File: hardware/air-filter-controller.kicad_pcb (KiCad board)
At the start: 4 copper layers, 41.1 x 138.8 mm, 126 parts, among them J1 TYPE-C-31-M-12, J10 Conn_01x04, J11 Conn_01x04, J12 Conn_01x04, J13 Conn_01x02, J14 Conn_01x02, J3 Conn_01x04, J4 Conn_01x03, J5 Conn_01x04, J6 Conn_01x04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

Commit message: Routing and placement done
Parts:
- added J2: Conn_01x05, Connector_PinHeader_2.54mm:PinHeader_1x05_P2.54mm_Vertical, F.Cu at (143.1, 72.1)
- moved H3 143.7 mm to (107.0, 176.8)
- moved J8 128.5 mm to (109.7, 169.8)
- moved H4 127.6 mm to (141.8, 176.8)
- moved J7 127.2 mm to (109.7, 157.8)
- moved R23 124.5 mm to (105.8, 153.3), turned to 180 degrees
- moved R26 123.8 mm to (105.8, 165.3), turned to 180 degrees
- moved R24 122.6 mm to (111.2, 165.3)
- moved R21 122.5 mm to (111.2, 153.3)
- moved R22 120.6 mm to (108.5, 153.5), turned to 180 degrees
- moved R25 120.1 mm to (108.5, 165.5), turned to 180 degrees
- moved D14 114.8 mm to (107.6, 150.7), turned to 180 degrees
- moved D17 114.4 mm to (107.6, 162.7), turned to 180 degrees
- moved D16 114.2 mm to (114.8, 162.7)
- moved D13 113.2 mm to (114.8, 150.7)
- moved R35 111.0 mm to (132.8, 146.8), turned to 90 degrees
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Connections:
- U1 pad 22: /SDI -> /SDO
- U1 pad 25: unconnected-(U1-IO48-Pad25) -> /PWM0
- U1 pad 32: unconnected-(U1-IO39-Pad32) -> /PWM1
- U1 pad 36: unconnected-(U1-RXD0-Pad36) -> /RXD0
- U1 pad 37: unconnected-(U1-TXD0-Pad37) -> /TXD0
- U1 pad 8: /SDO -> /SDI
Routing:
- net +12V: track 19.8 -> 355.1 mm, vias 0 -> 14
- net +3V3: track 32.7 -> 298.2 mm, vias 0 -> 23
- net /FAN_GND: track 4.49 -> 235.2 mm, vias 0 -> 9
- net /PWM0: track 3.95 -> 132.9 mm, vias 0 -> 4
- net /PWM1: track 0.00 -> 122.9 mm, vias 0 -> 2
- net /TACH4: track 0.00 -> 121.4 mm, vias 0 -> 4
- net /TACH3: track 0.00 -> 114.1 mm, vias 0 -> 4
- net /TACH8: track 0.00 -> 108.1 mm, vias 0 -> 6
- net /TACH2: track 0.00 -> 102.2 mm, vias 0 -> 4
- net GND: track 24.5 -> 122.2 mm, vias 0 -> 413
- net /TACH7: track 0.00 -> 94.6 mm, vias 0 -> 4
- net /TACH1: track 0.00 -> 90.0 mm, vias 0 -> 4
- net /TACH6: track 0.00 -> 84.8 mm, vias 0 -> 6
- net /TACH5: track 0.00 -> 73.1 mm, vias 0 -> 4
- net /TACH0: track 4.99 -> 71.6 mm, vias 0 -> 2
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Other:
- board size 41.1 x 138.8 mm -> 41 x 134.6 mm
- board text added: "air-filter-controller v1.0"

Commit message: Hardware v1.0
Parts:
- C8: value 47uF -> 22uF 25V
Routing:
- net Net-(U3-EN): track 2.82 -> 5.82 mm
- net GND: track 122.2 -> 121.3 mm
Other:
- board text added: "0"
- board text added: "1"
- board text added: "12V"
- board text added: "2"
- board text added: "3"
- board text added: "3V3"
- board text added: "4"
- board text added: "5"
- board text added: "5V-12V in 5.5mm/2.1mm Center positive"
- board text added: "6"
- board text added: "7"
- board text added: "8"
- board text added: "G"
- board text added: "GND"
- board text added: "JACK"
- board text added: "M3 x4"
- board text added: "POWER"
- board text added: "PWM"
- board text added: "RX"
- board text added: "SW2"
- board text added: "SW3"
- board text added: "TACH"
- board text added: "TX"
- board text added: "USB"

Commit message: v1.1: start updating layout
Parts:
- removed C6: 100nF, Capacitor_SMD:C_0402_1005Metric
- removed LED1: HL-AF-5060H271BU46FU79GC-S1-THL, Homebrew:LED-ARRAY-SMD_6P-L5.4-W5.0-TL-FD
- removed U2: BMP280, Package_LGA:Bosch_LGA-8_2x2.5mm_P0.65mm_ClockwisePinNumbering
- added C14: 100nF, Capacitor_SMD:C_0402_1005Metric, F.Cu at (136.4, 60.1)
- added C15: 47uF, Capacitor_SMD:C_1206_3216Metric, F.Cu at (132.6, 90.0)
- added C16: 100nF, Capacitor_SMD:C_0402_1005Metric, F.Cu at (134.3, 90.0)
- added C17: 47uF, Capacitor_SMD:C_1206_3216Metric, F.Cu at (97.6, 82.8)
- added C18: 100nF, Capacitor_SMD:C_0402_1005Metric, F.Cu at (91.5, 84.8)
- added D37: WS2812B-2020, Homebrew:LED-SMD_4P-L2.0-W2.0-TL_WS2812B-2020, F.Cu at (136.8, 52.6)
- added D38: WS2812B-2020, Homebrew:LED-SMD_4P-L2.0-W2.0-TL_WS2812B-2020, F.Cu at (136.8, 55.5)
- added D39: WS2812B-2020, Homebrew:LED-SMD_4P-L2.0-W2.0-TL_WS2812B-2020, F.Cu at (136.8, 58.2)
- added D40: SMAJ5.0A, Diode_SMD:D_SMA, F.Cu at (173.5, 126.2)
- added D41: SMAJ5.0A, Diode_SMD:D_SMA, F.Cu at (140.2, 89.9)
- added D42: D, Diode_SMD:D_SMA, F.Cu at (173.5, 135.3)
- added D43: SMAJ5.0A, Diode_SMD:D_SMA, F.Cu at (133.8, 190.7)
- added D44: SMAJ5.0A, Diode_SMD:D_SMA, F.Cu at (130.1, 196.4)
- added D45: D_TVS 12V, Diode_SMD:D_SMA, F.Cu at (141.1, 191.8)
- added H5: Strain Relief, Homebrew:3_pin_2.54mm_pitch_strain_relief, F.Cu at (143.6, 90.0)
- added J15: Conn_01x03, Connector_PinHeader_2.54mm:PinHeader_1x03_P2.54mm_Vertical, F.Cu at (136.6, 87.4)
- added J16: Conn_01x08, easyeda2kicad:CONN-TH_8P-P1.25_HCTL_HC-1.25-8A, F.Cu at (184.0, 125.8)
- added J17: Conn_01x08, easyeda2kicad:CONN-TH_8P-P1.25_HCTL_HC-1.25-8A, F.Cu at (184.0, 130.2)
- added R48: 100, Resistor_SMD:R_0603_1608Metric_Pad0.98x0.95mm_HandSolder, F.Cu at (167.2, 125.2)
- added R49: 100, Resistor_SMD:R_0603_1608Metric_Pad0.98x0.95mm_HandSolder, F.Cu at (167.2, 127.7)
- added R50: 100, Resistor_SMD:R_0603_1608Metric_Pad0.98x0.95mm_HandSolder, F.Cu at (167.2, 130.2)
- added R51: 100, Resistor_SMD:R_0603_1608Metric_Pad0.98x0.95mm_HandSolder, F.Cu at (167.2, 132.7)
- added R52: 100, Resistor_SMD:R_0603_1608Metric_Pad0.98x0.95mm_HandSolder, F.Cu at (167.2, 135.2)
- added R53: 100, Resistor_SMD:R_0603_1608Metric_Pad0.98x0.95mm_HandSolder, F.Cu at (167.2, 137.7)
- added U4: AMS1117-3.3, Package_TO_SOT_SMD:SOT-223-3_TabPin2, F.Cu at (91.0, 90.8)
- added U5: ZX-SH1.0-4PWT, easyeda2kicad:CONN-SMD_4P-P1.00_MEGASTAR_ZX-SH1.0-4PWT, F.Cu at (173.2, 140.6)
- D35: value SMAJ5.0A -> WS2812B-2020; footprint Diode_SMD:D_SMA -> Homebrew:LED-SMD_4P-L2.0-W2.0-TL_WS2812B-2020
- J4: value Conn_01x03 -> Conn_01x04; footprint Connector_PinHeader_2.54mm:PinHeader_1x03_P2.54mm_Vertical -> Homebrew:CONN-TH_47053-1000
- L1: value 27uH -> 100uH
- R3: value 10 -> 220
- R4: value 10 -> 100k
- R46: value 47 -> 220
- R5: value 10 -> 1k; footprint Resistor_SMD:R_0603_1608Metric_Pad0.98x0.95mm_HandSolder -> Resistor_SMD:R_0402_1005Metric
- R8: value 22k 1% -> 16k 1%
- R9: value 100k 1% -> 110k 1%
- moved R4 140.6 mm to (132.7, 194.9), turned to -90 degrees
- moved R5 140.3 mm to (136.5, 193.0)
- moved R46 131.9 mm to (132.7, 198.3), turned to 90 degrees
- moved J4 121.9 mm to (139.1, 197.3), turned to 0 degrees
- moved D35 54.1 mm to (136.7, 49.9), turned to 0 degrees
- moved C7 42.4 mm to (88.2, 84.3), turned to -90 degrees
- moved D21 27.5 mm to (141.1, 143.8)
- moved D33 27.5 mm to (110.8, 136.3)
- moved D34 27.5 mm to (138.0, 136.3)
- moved J5 27.5 mm to (109.6, 149.3)
- moved J9 27.5 mm to (139.1, 149.3)
- moved R14 27.5 mm to (105.7, 144.8)
- moved R15 27.5 mm to (111.1, 144.8)
- moved R44 27.5 mm to (108.5, 135.1)
- moved D10 27.5 mm to (114.7, 166.2)
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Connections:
- BUZZER1 pad 1: Net-(BUZZER1-Pad1) -> /BUZZER
- C10 pad 2: +3V3 -> +5V
- C11 pad 1: +3V3 -> +5V
- C12 pad 1: +3V3 -> +5V
- C7 pad 1: GND -> +5V
- C7 pad 2: +3V3 -> GND
- D35 pad 1: /BOOT -> +5V
- D35 pad 2: GND -> Net-(D35-DOUT)
- F1 pad 1: Net-(J4-Pin_2) -> /12V_RAW
- J2 pad 5: +12V -> +5V
- J4 pad 1: /12V_RAW -> /FAN_GND
- J4 pad 2: Net-(J4-Pin_2) -> +12V
- J4 pad 3: /VBUS_RAW -> Net-(J4-Pin_3)
- L1 pad 2: +3V3 -> +5V
- R3 pad 1: /LED_G -> Net-(D39-DOUT)
- R3 pad 2: Net-(LED1-A-Pad1) -> /LED_OUT
- R4 pad 1: /LED_R -> /TACH9
- R4 pad 2: Net-(LED1-A-Pad2) -> +3V3
- R46 pad 1: Net-(BUZZER1-Pad1) -> /PWM1
- R46 pad 2: /BUZZER -> Net-(J4-Pin_4)
- R5 pad 1: /LED_B -> /TACH9
- R5 pad 2: Net-(LED1-A-Pad3) -> Net-(J4-Pin_3)
- R9 pad 1: +3V3 -> +5V
- U1 pad 10: /12V_DIVIDED -> /PM0_RX
- U1 pad 13: /USB_DP -> /USB_DN
- U1 pad 14: /USB_DN -> /USB_DP
- U1 pad 16: unconnected-(U1-IO46-Pad16) -> /PM_SENSOR_ENABLE
- U1 pad 21: /SCK -> /TACH9
- U1 pad 22: /SDO -> /PM0_TX
- U1 pad 26: unconnected-(U1-IO45-Pad26) -> /SW0
- U1 pad 33: /LED_G -> /LED_SIGNAL
- U1 pad 34: /LED_R -> /SDA
- U1 pad 35: /LED_B -> /SCL
- U1 pad 39: /SW0 -> /12V_DIVIDED
- U1 pad 8: /SDI -> /PM1_RX
- U1 pad 9: /CSB -> /PM1_TX
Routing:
- net +3V3: track 298.2 -> 168.9 mm, vias 23 -> 20
- net /TACH9: track 0.00 -> 118.1 mm, vias 0 -> 4
- net +5V: track 0.00 -> 92.9 mm, vias 0 -> 6
- net /BOOT: track 56.7 -> 0.00 mm, vias 4 -> 0
- net /SW0: track 56.0 -> 3.84 mm, vias 2 -> 0
- net Net-(Q1-G): track 46.2 -> 0.00 mm, vias 4 -> 0
- net /LED_OUT: track 0.00 -> 34.9 mm, vias 0 -> 2
- net /SW1: track 56.8 -> 24.7 mm, vias 2 -> 1
- net /TXD0: track 27.9 -> 0.00 mm, vias 1 -> 0
- net /FAN_GND: track 235.2 -> 261.2 mm, vias 9 -> 10
- net +12V: track 355.1 -> 329.8 mm, vias 14 -> 10
- net /SDI: track 23.6 -> 0.00 mm, vias 2 -> 0
- net /CSB: track 21.9 -> 0.00 mm, vias 2 -> 0
- net /RXD0: track 27.2 -> 5.84 mm, vias 2 -> 1
- net GND: track 121.3 -> 141.5 mm, vias 413 -> 47
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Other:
- board size 41 x 134.6 mm -> 41.1 x 163.6 mm
- board text added: "9"
- board text added: "air-filter-controller v1.1"
- board text removed: "air-filter-controller v1.0"

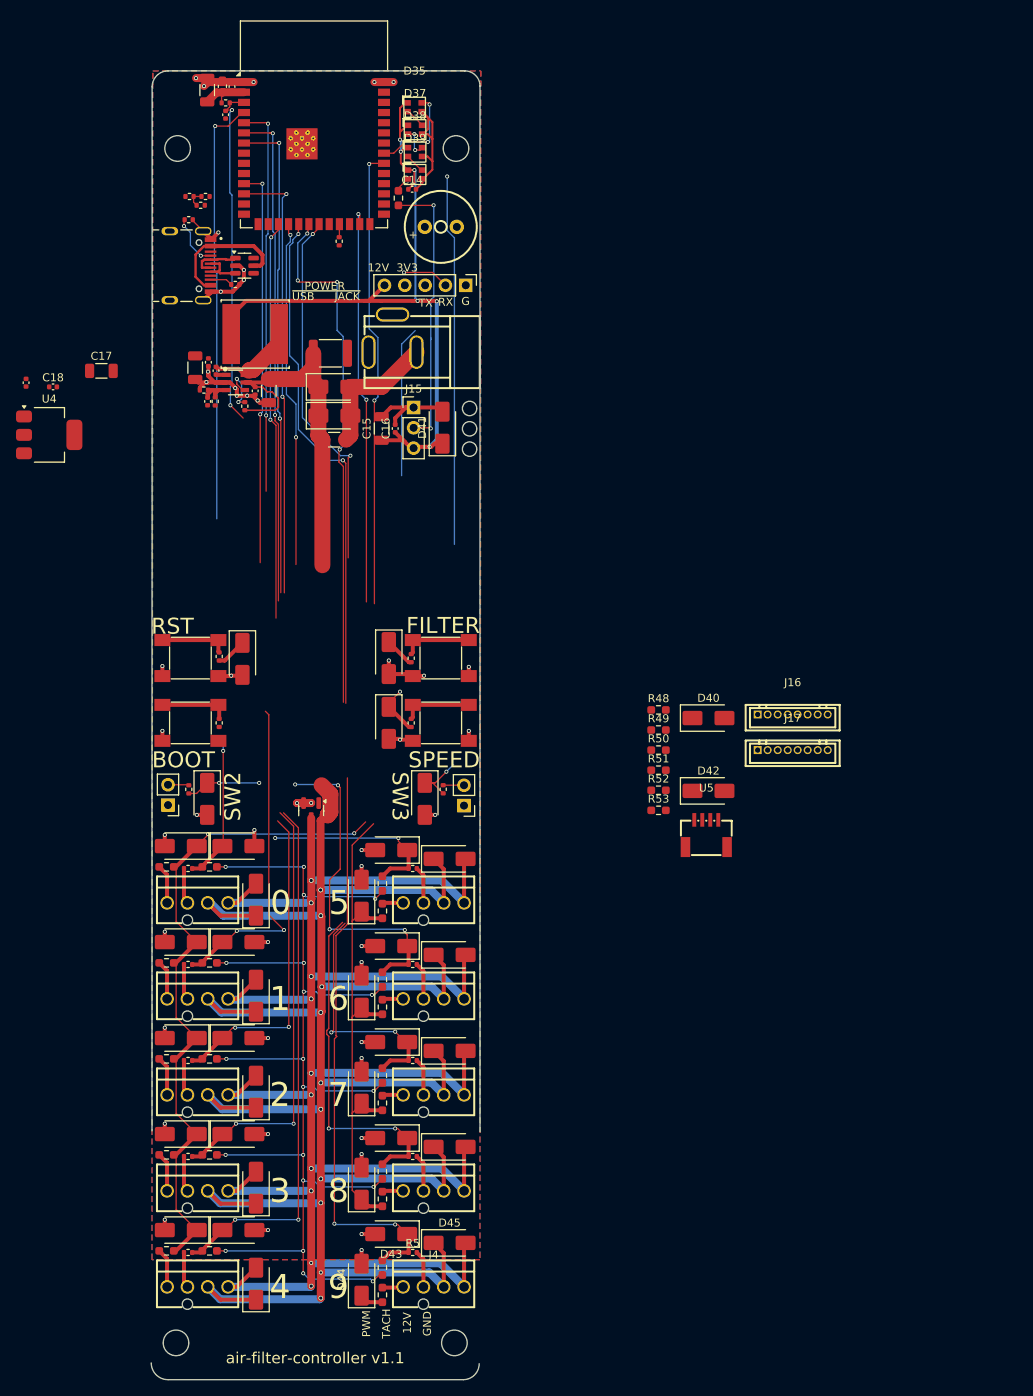
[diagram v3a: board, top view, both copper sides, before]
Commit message: Hardware revision v1.1:
- Fix flipped USB lines
- Remove diode on BOOT switch
- Remove buzzer resistor
- Change voltage divider to ADC channel 1
- Increased from 9 to 10 fan channels
- Switched to addressable LEDs
- Added connector for offboard WS2812 LEDs
- Added a Qwiic connector
- Added two connectors for PMS5003 particle sensors
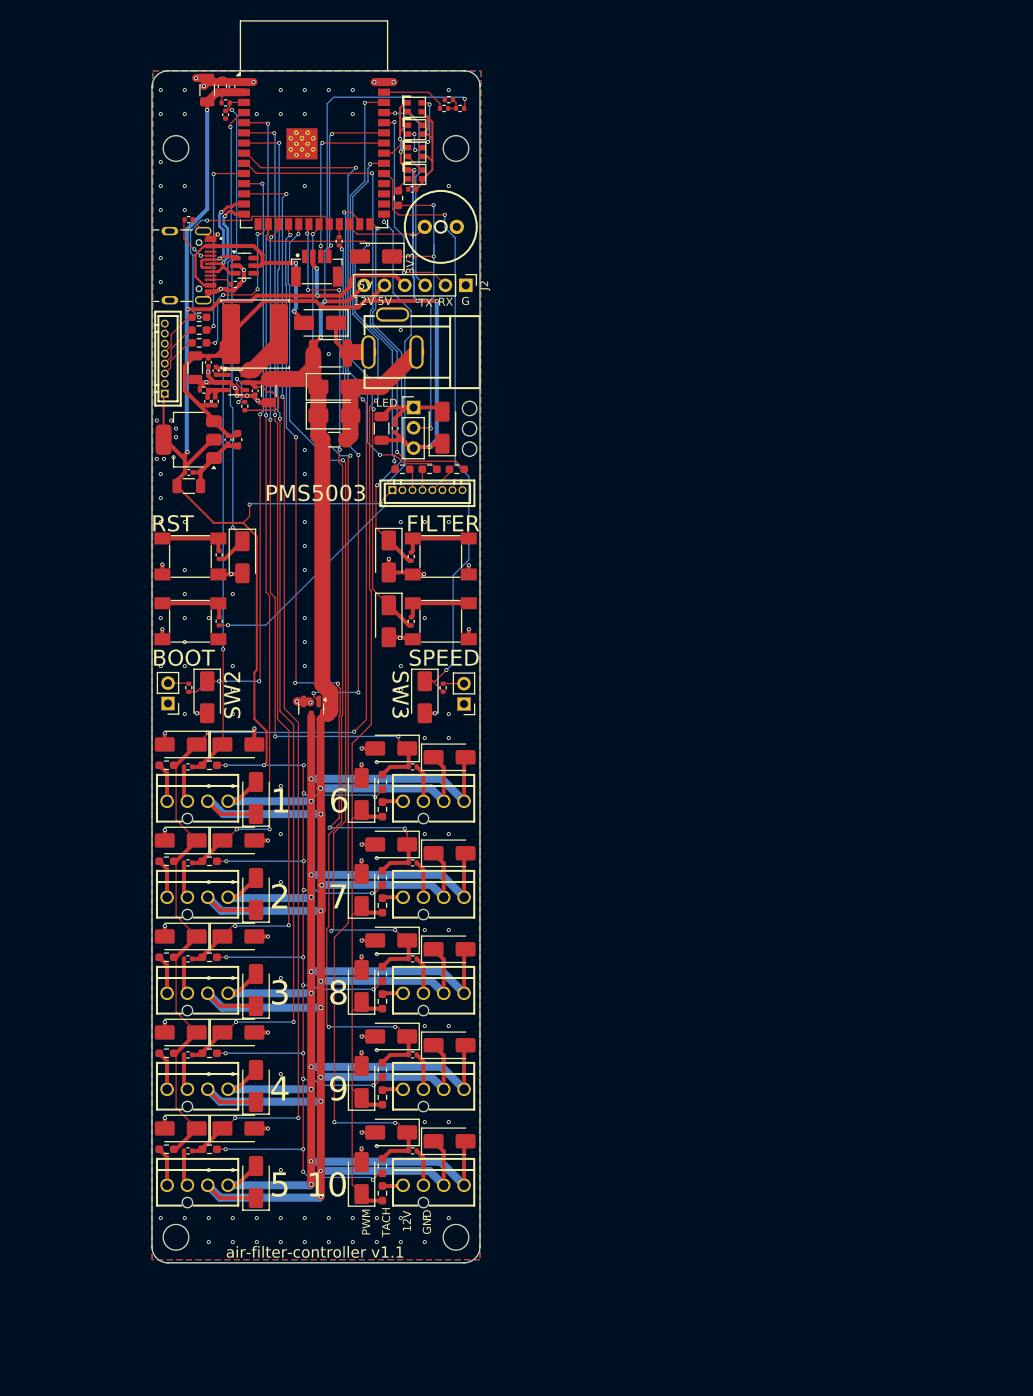
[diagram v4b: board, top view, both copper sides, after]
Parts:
- added C6: 10uF, Capacitor_SMD:C_0603_1608Metric, F.Cu at (114.6, 91.4)
- J16, J17: footprint easyeda2kicad:CONN-TH_8P-P1.25_HCTL_HC-1.25-8A -> Homebrew:CONN-TH_8P-P1.25_HCTL_HC-1.25-8A
- J2: value Conn_01x05 -> Conn_01x06; footprint Connector_PinHeader_2.54mm:PinHeader_1x05_P2.54mm_Vertical -> Connector_PinHeader_2.54mm:PinHeader_1x06_P2.54mm_Vertical
- U5: value ZX-SH1.0-4PWT -> HC-1.0-4PLT; footprint easyeda2kicad:CONN-SMD_4P-P1.00_MEGASTAR_ZX-SH1.0-4PWT -> Homebrew:CONN-SMD_4P-P1.00_HC-1.0-4PLT
- moved J16 90.2 mm to (105.5, 81.3), turned to 90 degrees
- moved U5 86.0 mm to (124.5, 69.8)
- moved R50 78.9 mm to (109.8, 76.1), turned to 180 degrees
- moved R49 76.1 mm to (109.8, 77.7), turned to 180 degrees
- moved D42 76.0 mm to (124.9, 76.8), turned to 180 degrees
- moved R48 73.5 mm to (109.8, 79.3), turned to 180 degrees
- moved D40 71.1 mm to (131.9, 68.5), turned to 180 degrees
- moved J17 56.0 mm to (138.3, 97.7)
- moved R53 49.5 mm to (142.0, 95.1), turned to 180 degrees
- moved R51 49.4 mm to (135.2, 95.1)
- moved R52 49.3 mm to (138.6, 95.1), turned to 180 degrees
- moved R41 35.6 mm to (142.4, 50.0), turned to 180 degrees
- moved R42 33.7 mm to (141.0, 48.9), turned to 180 degrees
- moved R43 31.8 mm to (140.4, 50.0), turned to 180 degrees
- moved C7 26.2 mm to (113.4, 91.4)
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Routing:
- net +3V3: track 168.9 -> 332.7 mm, vias 20 -> 28
- net +12V: track 329.8 -> 401.0 mm, vias 10 -> 13
- net /PM_SENSOR_ENABLE: track 0.00 -> 66.4 mm, vias 0 -> 6
- net /BOOT: track 0.00 -> 66.1 mm, vias 0 -> 2
- net Net-(Q1-G): track 0.00 -> 63.7 mm, vias 0 -> 4
- net /PM1_TX: track 0.00 -> 61.9 mm, vias 0 -> 2
- net /PM1_RX: track 0.00 -> 60.3 mm, vias 0 -> 2
- net /SW1: track 24.7 -> 71.9 mm, vias 1 -> 2
- net /SW0: track 3.84 -> 47.8 mm, vias 0 -> 2
- net /PM0_TX: track 0.00 -> 30.6 mm, vias 0 -> 2
- net /PWM1: track 125.9 -> 156.3 mm
- net /TXD0: track 0.00 -> 25.7 mm, vias 0 -> 1
- net +5V: track 92.9 -> 118.1 mm
- net /PM0_RX: track 0.00 -> 23.5 mm, vias 0 -> 2
- net /SW3: track 53.8 -> 77.0 mm
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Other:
- board size 41.1 x 163.6 mm -> 41 x 149 mm
- board text added: "10"
- board text added: "5V"
- board text added: "LED"
- board text added: "LED_OUT"
- board text added: "PMS5003"
- board text added: "{ "ViaStitching": "0.2", "stitch_zone_0": { "HSpacing": "3", "VSpacing": "3", "Clearance": "1", "Randomize": false } }"
- board text removed: "0"
- board text removed: "JACK"
- board text removed: "POWER"
- board text removed: "USB"

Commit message: Hardware v1.1
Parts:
- added C19: 10uF, Capacitor_SMD:C_0603_1608Metric, F.Cu at (118.0, 85.3)
- added C20: 22uF 25V, Capacitor_SMD:C_1206_3216Metric, F.Cu at (123.7, 121.9)
- added C22: 220uF, Capacitor_SMD:CP_Elec_8x10, F.Cu at (125.5, 99.0)
- added C23: 22uF 25V, Capacitor_SMD:C_1206_3216Metric, F.Cu at (117.9, 95.7)
- added C24: 10uF, Capacitor_SMD:C_0603_1608Metric, F.Cu at (119.4, 136.2)
- added C25: 10uF, Capacitor_SMD:C_0603_1608Metric, F.Cu at (119.4, 148.2)
- added C26: 10uF, Capacitor_SMD:C_0603_1608Metric, F.Cu at (119.4, 160.5)
- added C27: 10uF, Capacitor_SMD:C_0603_1608Metric, F.Cu at (119.4, 172.5)
- added C28: 10uF, Capacitor_SMD:C_0603_1608Metric, F.Cu at (119.4, 184.4)
- added C29: 10uF, Capacitor_SMD:C_0603_1608Metric, F.Cu at (141.6, 128.6)
- added C30: 10uF, Capacitor_SMD:C_0603_1608Metric, F.Cu at (141.2, 140.6)
- added C31: 10uF, Capacitor_SMD:C_0603_1608Metric, F.Cu at (141.6, 152.6)
- added C32: 10uF, Capacitor_SMD:C_0603_1608Metric, F.Cu at (141.2, 164.6)
- added C33: 10uF, Capacitor_SMD:C_0603_1608Metric, F.Cu at (141.1, 176.6)
- added C34: 100nF, Capacitor_SMD:C_0402_1005Metric, F.Cu at (126.6, 93.1)
- added L2: 4.7uH, Inductor_SMD:L_Sunlord_SWPA4030S, F.Cu at (120.7, 92.1)
- moved C8 1.40 mm to (119.9, 85.3)
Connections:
- C5 pad 1: +12V -> /12V_PREFILTER
- D1 pad 1: +12V -> /12V_PREFILTER
- D2 pad 1: +12V -> /12V_PREFILTER
- F1 pad 2: +12V -> /12V_PREFILTER
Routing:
- net +12V: track 401.0 -> 465.6 mm
- net /FAN_GND: track 260.9 -> 313.2 mm
- net /12V_PREFILTER: track 0.00 -> 39.1 mm
- net GND: track 154.5 -> 165.4 mm, vias 165 -> 158
- net /TACH1: track 102.2 -> 104.7 mm
- net +3V3: track 332.7 -> 334.1 mm
- net /TACH7: track 109.2 -> 108.3 mm
- net /TACH6: track 99.7 -> 98.8 mm
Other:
- board text removed: "{ "ViaStitching": "0.2", "stitch_zone_0": { "HSpacing": "3", "VSpacing": "3", "Clearance": "1", "Randomize": false } }"
